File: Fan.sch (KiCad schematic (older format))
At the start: 9 parts

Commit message: 3.9 Understanding The Arduino Module Added content to Arduino and block (header) modules
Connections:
- net labels added: CURR_MEAS, FAN_EN_N, FAN_OUT+, FAN_OUT-, TACH_IN, TACH_MEAS
- net labels removed: Current Sense, Fan_In, Power+, Power-, Tach, Tach_Out
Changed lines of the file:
@@
 Sheet 8 9
 Title ""
-Date "8 feb 2014"
+Date "10 feb 2014"
 Rev ""
 Comp ""
@@
 $EndDescr
 Text HLabel 10350 3350 2    60   Output ~ 0
-Power+
-Text HLabel 10350 3550 2    60   Input ~ 0
-Power-
+FAN_OUT+
+Text HLabel 10350 3550 2    60   Output ~ 0
+FAN_OUT-
 Text HLabel 10350 3750 2    60   Input ~ 0
-Tach
+TACH_IN
 Text HLabel 1250 4350 0    60   Output ~ 0
-Tach_Out
+TACH_MEAS
 Text HLabel 1250 4000 0    60   Input ~ 0
-Fan_In
+FAN_EN_N
 $Comp
 L LM324 U?
@@
 	8700 5500 2400 5500
 Text HLabel 1250 4200 0    60   Output ~ 0
-Current Sense
+CURR_MEAS
 Connection ~ 4350 3600
 $Comp

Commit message: 3.10   Revisiting The Current/Fan Module End of Module 3, lots of cleanup/changes all over the place.
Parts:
- removed R? (x3): R, symbol R
- removed RV?: POT, symbol POT
- added D?: DIODE, ~, symbol DIODE
- added Q? (x2): MOSFET_N, ~, symbol MOSFET_N
- added TH?: THERMISTOR, ~, symbol THERMISTOR
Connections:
- net labels added: FAN_MODE, FAN_PWN
- net labels removed: FAN_EN_N
- wire segments 30 -> 29
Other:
- moved on the sheet: R?, U?

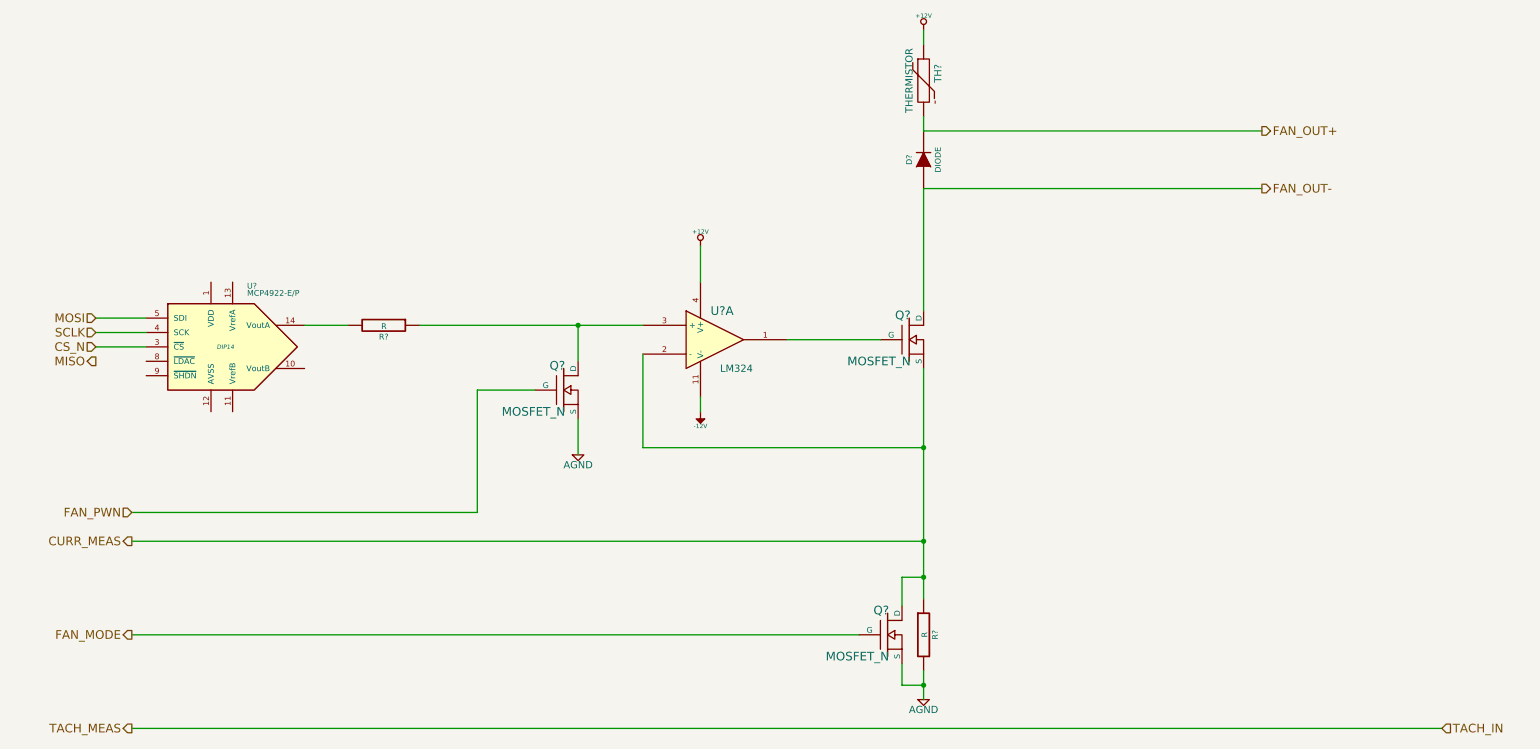
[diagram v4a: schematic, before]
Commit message: 5.3 Video 1/2 Associating and Placing the Relay Module
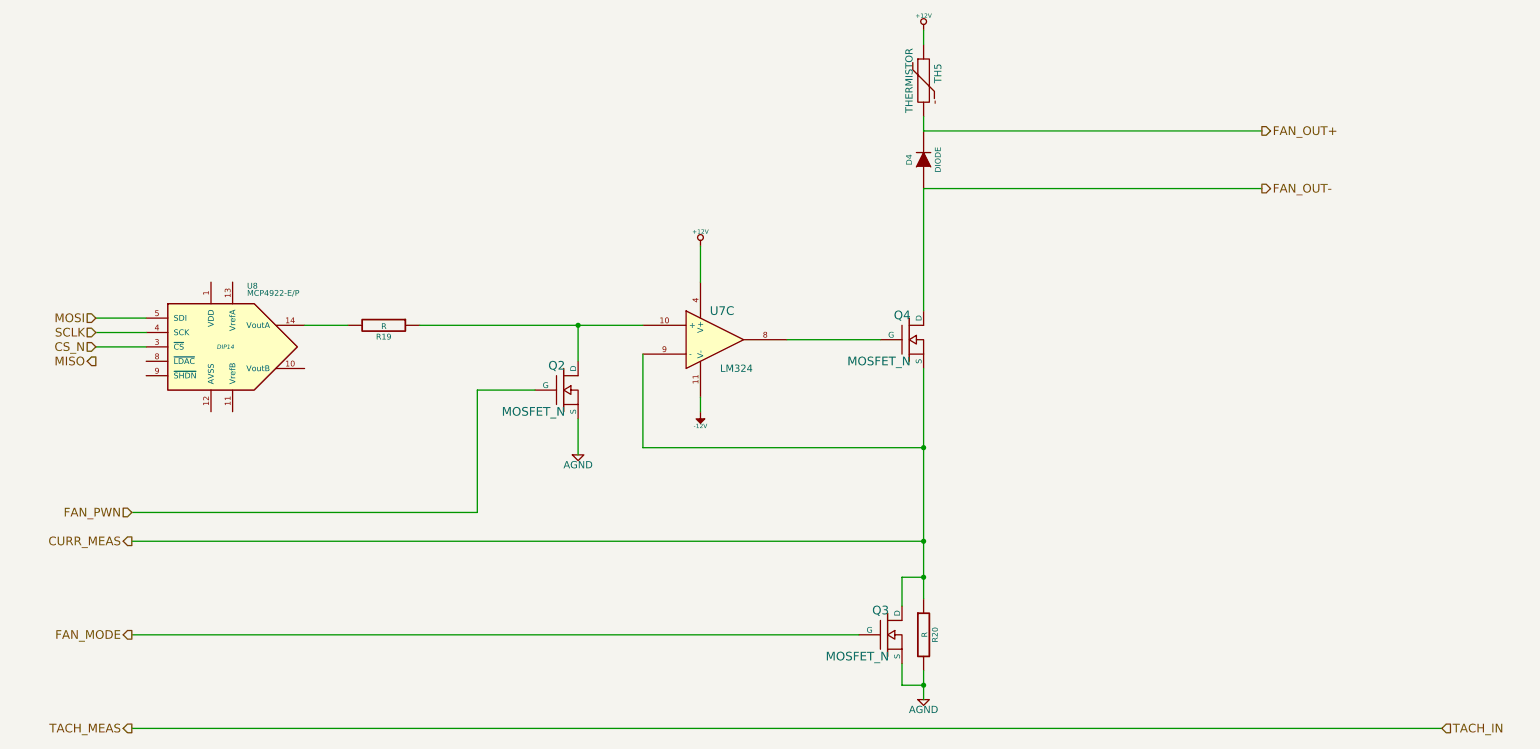
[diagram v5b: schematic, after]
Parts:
- gave numbers to parts that had none: 9
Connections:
- net CURR_MEAS: now also U7.9 (-); no longer U7.2 (-)
- net at Q4.G: now also U7.8; no longer U7.1
- net at Q2.D, R19.1: now also U7.10 (+); no longer U7.3 (+)
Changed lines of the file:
@@
 Sheet 7 9
 Title ""
-Date "10 feb 2014"
+Date "19 feb 2014"
 Rev ""
 Comp ""
@@
 FAN_PWN
 $Comp
-L LM324 U?
-U 1 1 52F26B24
+L LM324 U7
+U 3 1 52F26B24
 P 5300 2800
-F 0 "U?" H 5350 3000 60  0000 C CNN
+F 0 "U7" H 5350 3000 60  0000 C CNN
 F 1 "LM324" H 5450 2600 50  0000 C CNN
 F 2 "" H 5300 2800 60  0000 C CNN
 F 3 "" H 5300 2800 60  0000 C CNN
-	1    5300 2800
-	1    0    0    -1
-$EndComp
-$Comp
-L MOSFET_N Q?
+	3    5300 2800
+	1    0    0    -1
+$EndComp
+$Comp
+L MOSFET_N Q4
 U 1 1 52F26B33
 P 6650 2800
-F 0 "Q?" H 6660 2970 60  0000 R CNN
+F 0 "Q4" H 6660 2970 60  0000 R CNN
 F 1 "MOSFET_N" H 6660 2650 60  0000 R CNN
 F 2 "" H 6650 2800 60  0000 C CNN
@@
 $EndComp
 $Comp
-L +12V #PWR?
+L +12V #PWR034
 U 1 1 52F26B42
 P 6750 650
-F 0 "#PWR?" H 6750 600 20  0001 C CNN
+F 0 "#PWR034" H 6750 600 20  0001 C CNN
 F 1 "+12V" H 6750 750 30  0000 C CNN
 F 2 "" H 6750 650 60  0000 C CNN
@@
 $EndComp
 $Comp
-L AGND #PWR?
+L AGND #PWR035
 U 1 1 52F26B7F
 P 6750 5300
-F 0 "#PWR?" H 6750 5300 40  0001 C CNN
+F 0 "#PWR035" H 6750 5300 40  0001 C CNN
 F 1 "AGND" H 6750 5230 50  0000 C CNN
 F 2 "" H 6750 5300 60  0000 C CNN
@@
 $EndComp
 $Comp
-L R R?
+L R R20
 U 1 1 52F26B8E
 P 6750 4850
-F 0 "R?" V 6830 4850 40  0000 C CNN
+F 0 "R20" V 6830 4850 40  0000 C CNN
 F 1 "R" V 6757 4851 40  0000 C CNN
 F 2 "" V 6680 4850 30  0000 C CNN
@@
 $EndComp
 $Comp
-L +12V #PWR?
+L +12V #PWR036
 U 1 1 52F26BE2
 P 5200 2150
-F 0 "#PWR?" H 5200 2100 20  0001 C CNN
+F 0 "#PWR036" H 5200 2100 20  0001 C CNN
 F 1 "+12V" H 5200 2250 30  0000 C CNN
 F 2 "" H 5200 2150 60  0000 C CNN
@@
 $EndComp
 $Comp
-L -12V #PWR?
+L -12V #PWR037
 U 1 1 52F26BF3
 P 5200 3300
-F 0 "#PWR?" H 5200 3430 20  0001 C CNN
+F 0 "#PWR037" H 5200 3430 20  0001 C CNN
 F 1 "-12V" H 5200 3400 30  0000 C CNN
 F 2 "" H 5200 3300 60  0000 C CNN
@@
 $EndComp
 $Comp
-L AGND #PWR?
+L AGND #PWR038
 U 1 1 52F26C6F
 P 4350 3600
-F 0 "#PWR?" H 4350 3600 40  0001 C CNN
+F 0 "#PWR038" H 4350 3600 40  0001 C CNN
 F 1 "AGND" H 4350 3530 50  0000 C CNN
 F 2 "" H 4350 3600 60  0000 C CNN
@@
 $EndComp
 $Comp
-L MCP4922-E/P U?
+L MCP4922-E/P U8
 U 1 1 52F26C9B
 P 1900 2850
-F 0 "U?" H 2050 3250 40  0000 L BNN
+F 0 "U8" H 2050 3250 40  0000 L BNN
 F 1 "MCP4922-E/P" H 2050 3200 40  0000 L BNN
 F 2 "DIP14" H 1900 2850 30  0000 C CIN
@@
 CURR_MEAS
 $Comp
-L R R?
+L R R19
 U 1 1 52F26DC7
 P 3000 2700
-F 0 "R?" V 3080 2700 40  0000 C CNN
+F 0 "R19" V 3080 2700 40  0000 C CNN
 F 1 "R" V 3007 2701 40  0000 C CNN
 F 2 "" V 2930 2700 30  0000 C CNN
@@
 SCLK
 $Comp
-L MOSFET_N Q?
+L MOSFET_N Q2
 U 1 1 52F82E27
 P 4250 3150
-F 0 "Q?" H 4260 3320 60  0000 R CNN
+F 0 "Q2" H 4260 3320 60  0000 R CNN
 F 1 "MOSFET_N" H 4260 3000 60  0000 R CNN
 F 2 "~" H 4250 3150 60  0000 C CNN
@@
 FAN_MODE
 $Comp
-L DIODE D?
+L DIODE D4
 U 1 1 52F82EC1
 P 6750 1550
-F 0 "D?" H 6750 1650 40  0000 C CNN
+F 0 "D4" H 6750 1650 40  0000 C CNN
 F 1 "DIODE" H 6750 1450 40  0000 C CNN
 F 2 "~" H 6750 1550 60  0000 C CNN
@@
 $EndComp
 $Comp
-L MOSFET_N Q?
+L MOSFET_N Q3
 U 1 1 52F82F64
 P 6500 4850
-F 0 "Q?" H 6510 5020 60  0000 R CNN
+F 0 "Q3" H 6510 5020 60  0000 R CNN
 F 1 "MOSFET_N" H 6510 4700 60  0000 R CNN
 F 2 "~" H 6500 4850 60  0000 C CNN
@@
 Connection ~ 6750 3550
 $Comp
-L THERMISTOR TH?
+L THERMISTOR TH5
 U 1 1 52F83066
 P 6750 1000
-F 0 "TH?" V 6850 1050 50  0000 C CNN
+F 0 "TH5" V 6850 1050 50  0000 C CNN
 F 1 "THERMISTOR" V 6650 1000 50  0000 C CNN
 F 2 "~" H 6750 1000 60  0000 C CNN

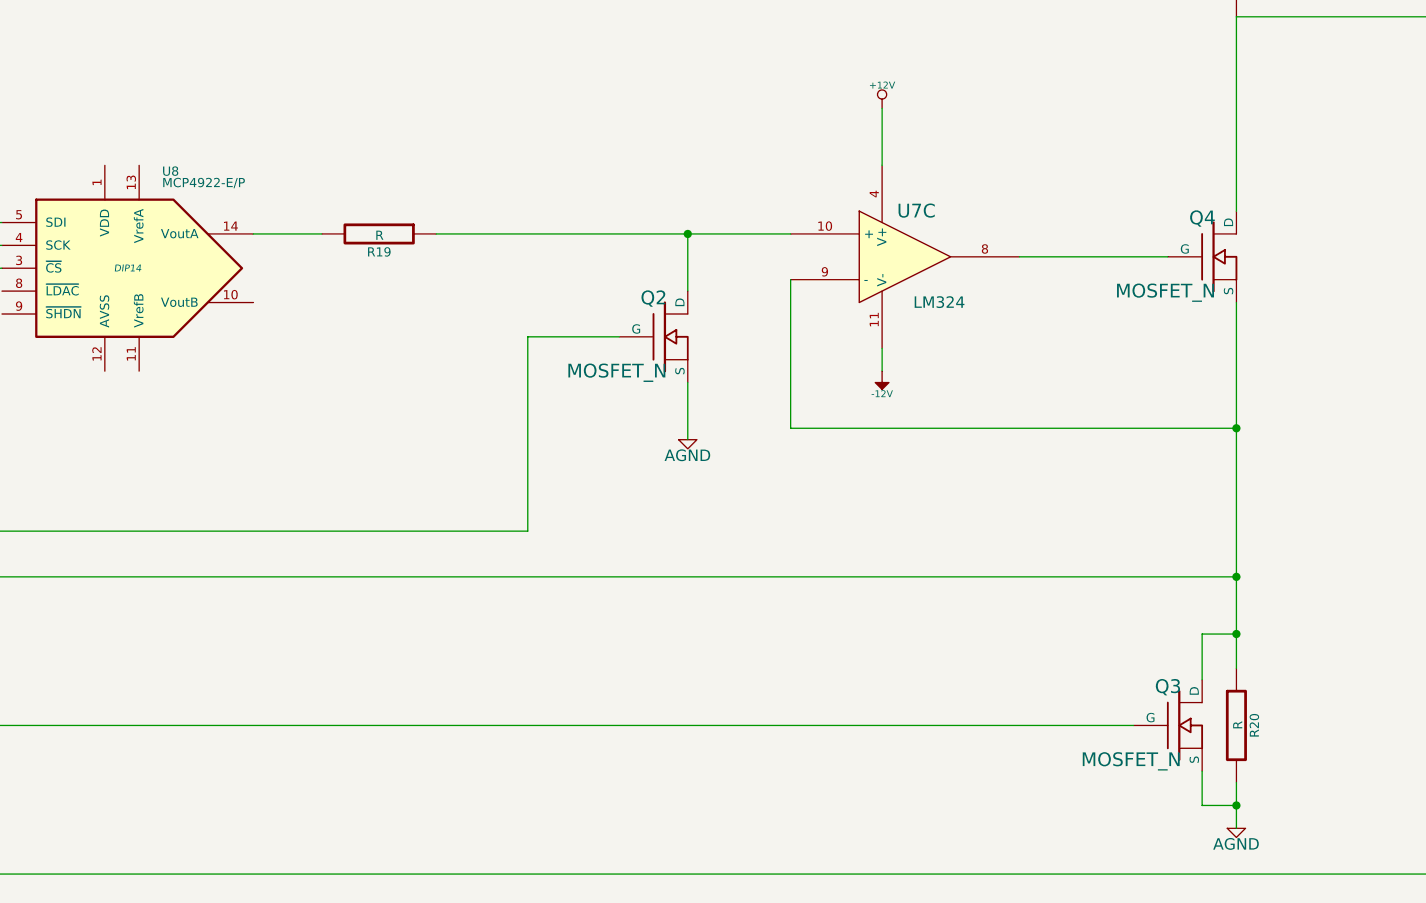
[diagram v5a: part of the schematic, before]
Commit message: 5.4 Video 1/2 Associating and Placing the Thermocouple Module
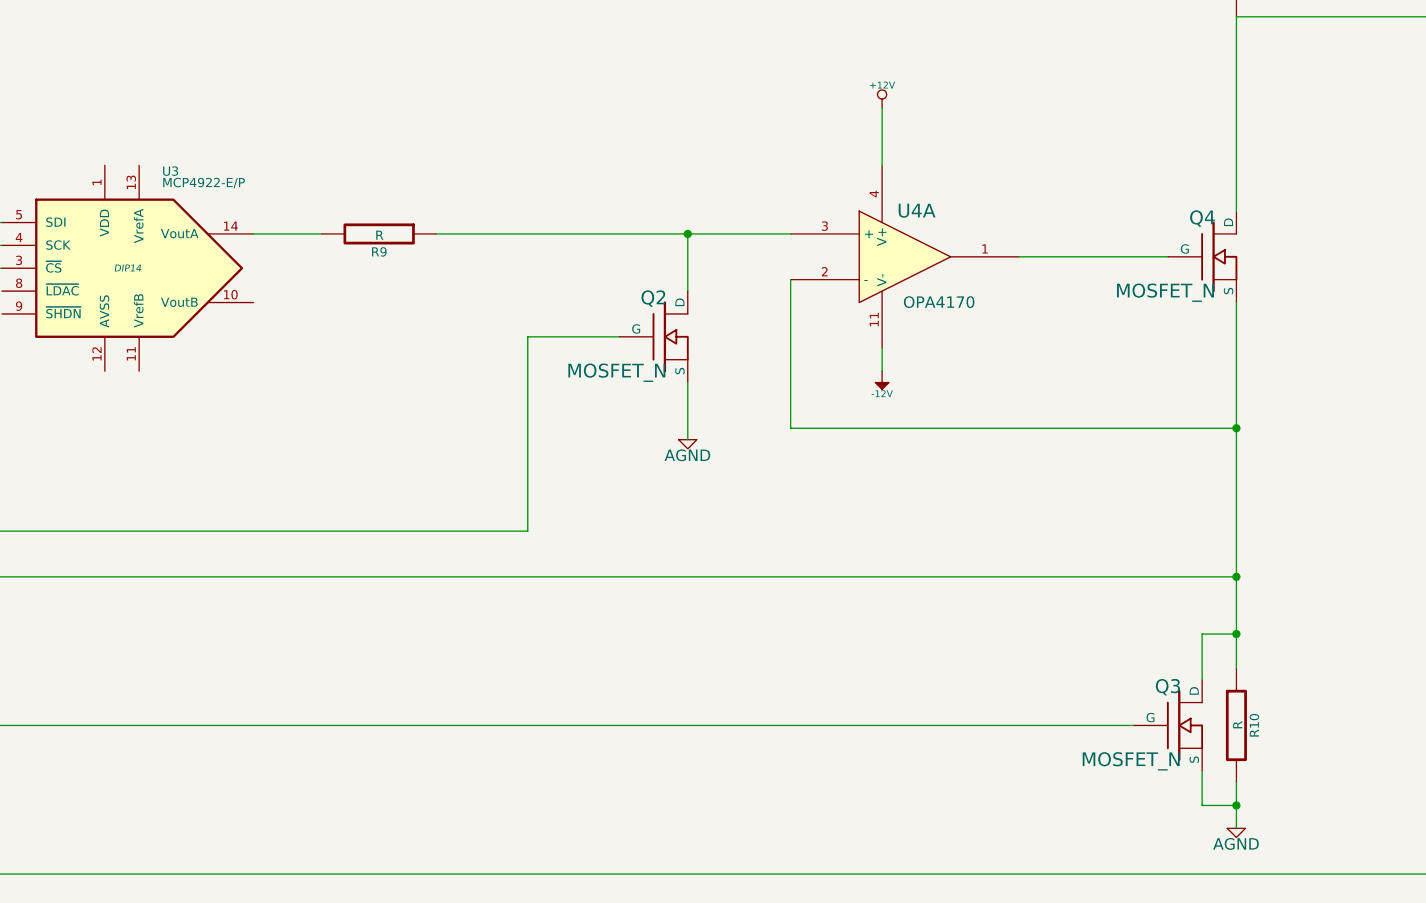
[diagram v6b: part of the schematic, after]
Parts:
- U4: renamed from U7; value LM324 -> OPA4170
- renumbered R20 to R10, R19 to R9, U8 to U3
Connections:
- net CURR_MEAS: now also U4.2 (-); no longer U4.9 (-)
- net at Q2.D, R9.1: now also U4.3 (+); no longer U4.10 (+)
- net at Q4.G: now also U4.1; no longer U4.8
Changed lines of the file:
@@
 $Descr A4 11693 8268
 encoding utf-8
-Sheet 7 9
+Sheet 6 9
 Title ""
-Date "19 feb 2014"
+Date "21 feb 2014"
 Rev ""
 Comp ""
@@
 FAN_PWN
 $Comp
-L LM324 U7
-U 3 1 52F26B24
+L LM324 U4
+U 1 1 52F26B24
 P 5300 2800
-F 0 "U7" H 5350 3000 60  0000 C CNN
-F 1 "LM324" H 5450 2600 50  0000 C CNN
+F 0 "U4" H 5350 3000 60  0000 C CNN
+F 1 "OPA4170" H 5450 2600 50  0000 C CNN
 F 2 "" H 5300 2800 60  0000 C CNN
 F 3 "" H 5300 2800 60  0000 C CNN
-	3    5300 2800
+	1    5300 2800
 	1    0    0    -1
 $EndComp
@@
 $EndComp
 $Comp
-L +12V #PWR034
+L +12V #PWR23
 U 1 1 52F26B42
 P 6750 650
-F 0 "#PWR034" H 6750 600 20  0001 C CNN
+F 0 "#PWR23" H 6750 600 20  0001 C CNN
 F 1 "+12V" H 6750 750 30  0000 C CNN
 F 2 "" H 6750 650 60  0000 C CNN
@@
 $EndComp
 $Comp
-L AGND #PWR035
+L AGND #PWR24
 U 1 1 52F26B7F
 P 6750 5300
-F 0 "#PWR035" H 6750 5300 40  0001 C CNN
+F 0 "#PWR24" H 6750 5300 40  0001 C CNN
 F 1 "AGND" H 6750 5230 50  0000 C CNN
 F 2 "" H 6750 5300 60  0000 C CNN
@@
 $EndComp
 $Comp
-L R R20
+L R R10
 U 1 1 52F26B8E
 P 6750 4850
-F 0 "R20" V 6830 4850 40  0000 C CNN
+F 0 "R10" V 6830 4850 40  0000 C CNN
 F 1 "R" V 6757 4851 40  0000 C CNN
 F 2 "" V 6680 4850 30  0000 C CNN
@@
 $EndComp
 $Comp
-L +12V #PWR036
+L +12V #PWR21
 U 1 1 52F26BE2
 P 5200 2150
-F 0 "#PWR036" H 5200 2100 20  0001 C CNN
+F 0 "#PWR21" H 5200 2100 20  0001 C CNN
 F 1 "+12V" H 5200 2250 30  0000 C CNN
 F 2 "" H 5200 2150 60  0000 C CNN
@@
 $EndComp
 $Comp
-L -12V #PWR037
+L -12V #PWR22
 U 1 1 52F26BF3
 P 5200 3300
-F 0 "#PWR037" H 5200 3430 20  0001 C CNN
+F 0 "#PWR22" H 5200 3430 20  0001 C CNN
 F 1 "-12V" H 5200 3400 30  0000 C CNN
 F 2 "" H 5200 3300 60  0000 C CNN
@@
 $EndComp
 $Comp
-L AGND #PWR038
+L AGND #PWR20
 U 1 1 52F26C6F
 P 4350 3600
-F 0 "#PWR038" H 4350 3600 40  0001 C CNN
+F 0 "#PWR20" H 4350 3600 40  0001 C CNN
 F 1 "AGND" H 4350 3530 50  0000 C CNN
 F 2 "" H 4350 3600 60  0000 C CNN
@@
 $EndComp
 $Comp
-L MCP4922-E/P U8
+L MCP4922-E/P U3
 U 1 1 52F26C9B
 P 1900 2850
-F 0 "U8" H 2050 3250 40  0000 L BNN
+F 0 "U3" H 2050 3250 40  0000 L BNN
 F 1 "MCP4922-E/P" H 2050 3200 40  0000 L BNN
 F 2 "DIP14" H 1900 2850 30  0000 C CIN
@@
 CURR_MEAS
 $Comp
-L R R19
+L R R9
 U 1 1 52F26DC7
 P 3000 2700
-F 0 "R19" V 3080 2700 40  0000 C CNN
+F 0 "R9" V 3080 2700 40  0000 C CNN
 F 1 "R" V 3007 2701 40  0000 C CNN
 F 2 "" V 2930 2700 30  0000 C CNN

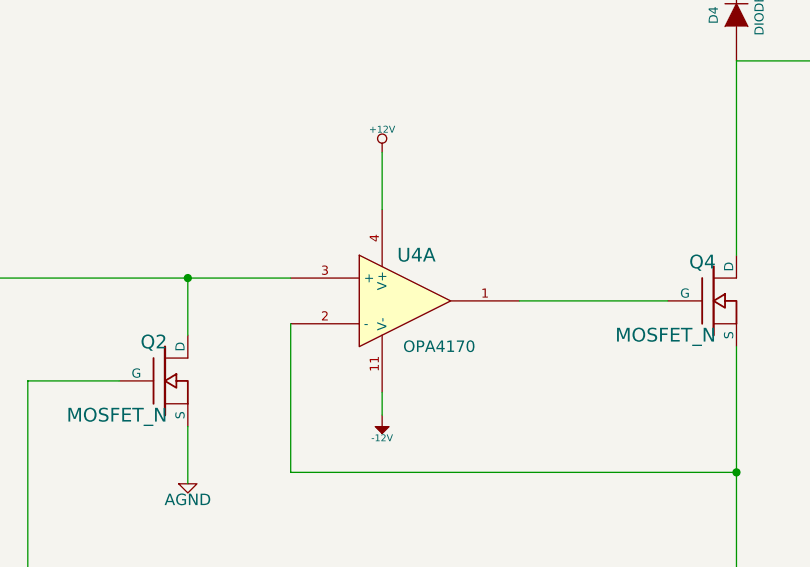
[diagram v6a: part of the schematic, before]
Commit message: 5.4 Video 2/2 Associating and Placing the Thermocouple Module
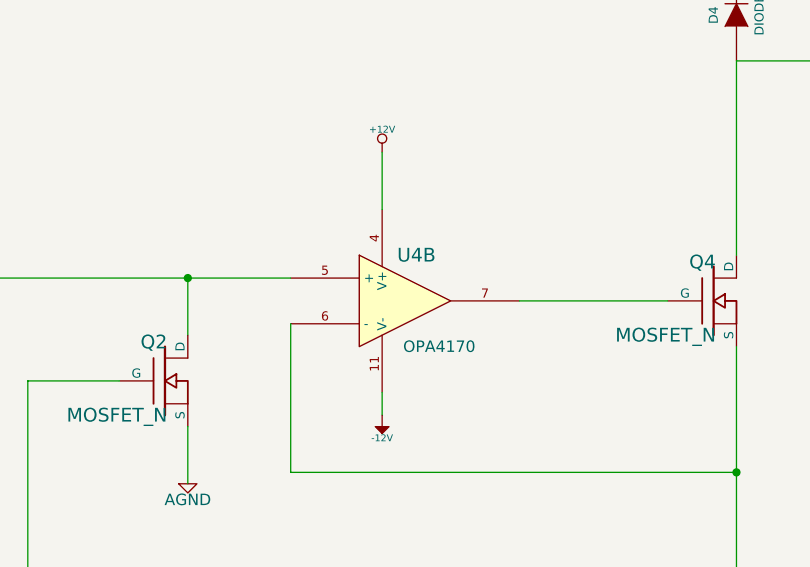
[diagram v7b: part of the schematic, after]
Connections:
- net CURR_MEAS: now also U4.6 (-); no longer U4.2 (-)
- net at Q4.G: now also U4.7; no longer U4.1
- net at Q2.D, R9.1: now also U4.5 (+); no longer U4.3 (+)
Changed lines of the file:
@@
 LIBS:BenchBudEE
 LIBS:BenchBudEE-cache
-EELAYER 27 0
+EELAYER 24 0
 EELAYER END
 $Descr A4 11693 8268
@@
 $Comp
 L LM324 U4
-U 1 1 52F26B24
+U 2 1 52F26B24
 P 5300 2800
 F 0 "U4" H 5350 3000 60  0000 C CNN
@@
 F 2 "" H 5300 2800 60  0000 C CNN
 F 3 "" H 5300 2800 60  0000 C CNN
-	1    5300 2800
+	2    5300 2800
 	1    0    0    -1
 $EndComp
@@
 $EndComp
 $Comp
-L +12V #PWR23
+L +12V #PWR020
 U 1 1 52F26B42
 P 6750 650
-F 0 "#PWR23" H 6750 600 20  0001 C CNN
+F 0 "#PWR020" H 6750 600 20  0001 C CNN
 F 1 "+12V" H 6750 750 30  0000 C CNN
 F 2 "" H 6750 650 60  0000 C CNN
@@
 $EndComp
 $Comp
-L AGND #PWR24
+L AGND #PWR021
 U 1 1 52F26B7F
 P 6750 5300
-F 0 "#PWR24" H 6750 5300 40  0001 C CNN
+F 0 "#PWR021" H 6750 5300 40  0001 C CNN
 F 1 "AGND" H 6750 5230 50  0000 C CNN
 F 2 "" H 6750 5300 60  0000 C CNN
@@
 $EndComp
 $Comp
-L +12V #PWR21
+L +12V #PWR022
 U 1 1 52F26BE2
 P 5200 2150
-F 0 "#PWR21" H 5200 2100 20  0001 C CNN
+F 0 "#PWR022" H 5200 2100 20  0001 C CNN
 F 1 "+12V" H 5200 2250 30  0000 C CNN
 F 2 "" H 5200 2150 60  0000 C CNN
@@
 $EndComp
 $Comp
-L -12V #PWR22
+L -12V #PWR023
 U 1 1 52F26BF3
 P 5200 3300
-F 0 "#PWR22" H 5200 3430 20  0001 C CNN
+F 0 "#PWR023" H 5200 3430 20  0001 C CNN
 F 1 "-12V" H 5200 3400 30  0000 C CNN
 F 2 "" H 5200 3300 60  0000 C CNN
@@
 $EndComp
 $Comp
-L AGND #PWR20
+L AGND #PWR024
 U 1 1 52F26C6F
 P 4350 3600
-F 0 "#PWR20" H 4350 3600 40  0001 C CNN
+F 0 "#PWR024" H 4350 3600 40  0001 C CNN
 F 1 "AGND" H 4350 3530 50  0000 C CNN
 F 2 "" H 4350 3600 60  0000 C CNN
